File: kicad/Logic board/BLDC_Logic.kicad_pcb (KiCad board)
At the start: 2 copper layers, 82.2 x 79.8 mm, 46 parts, among them J1 CONN_01X03, J10 Encdr Pwr, J11 3ph board, J12 3v3 output, J13 3v3 output, J2 CMD inputs, J3 IO, J4 CONN_01X03, J5 5V output, J6 5V output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

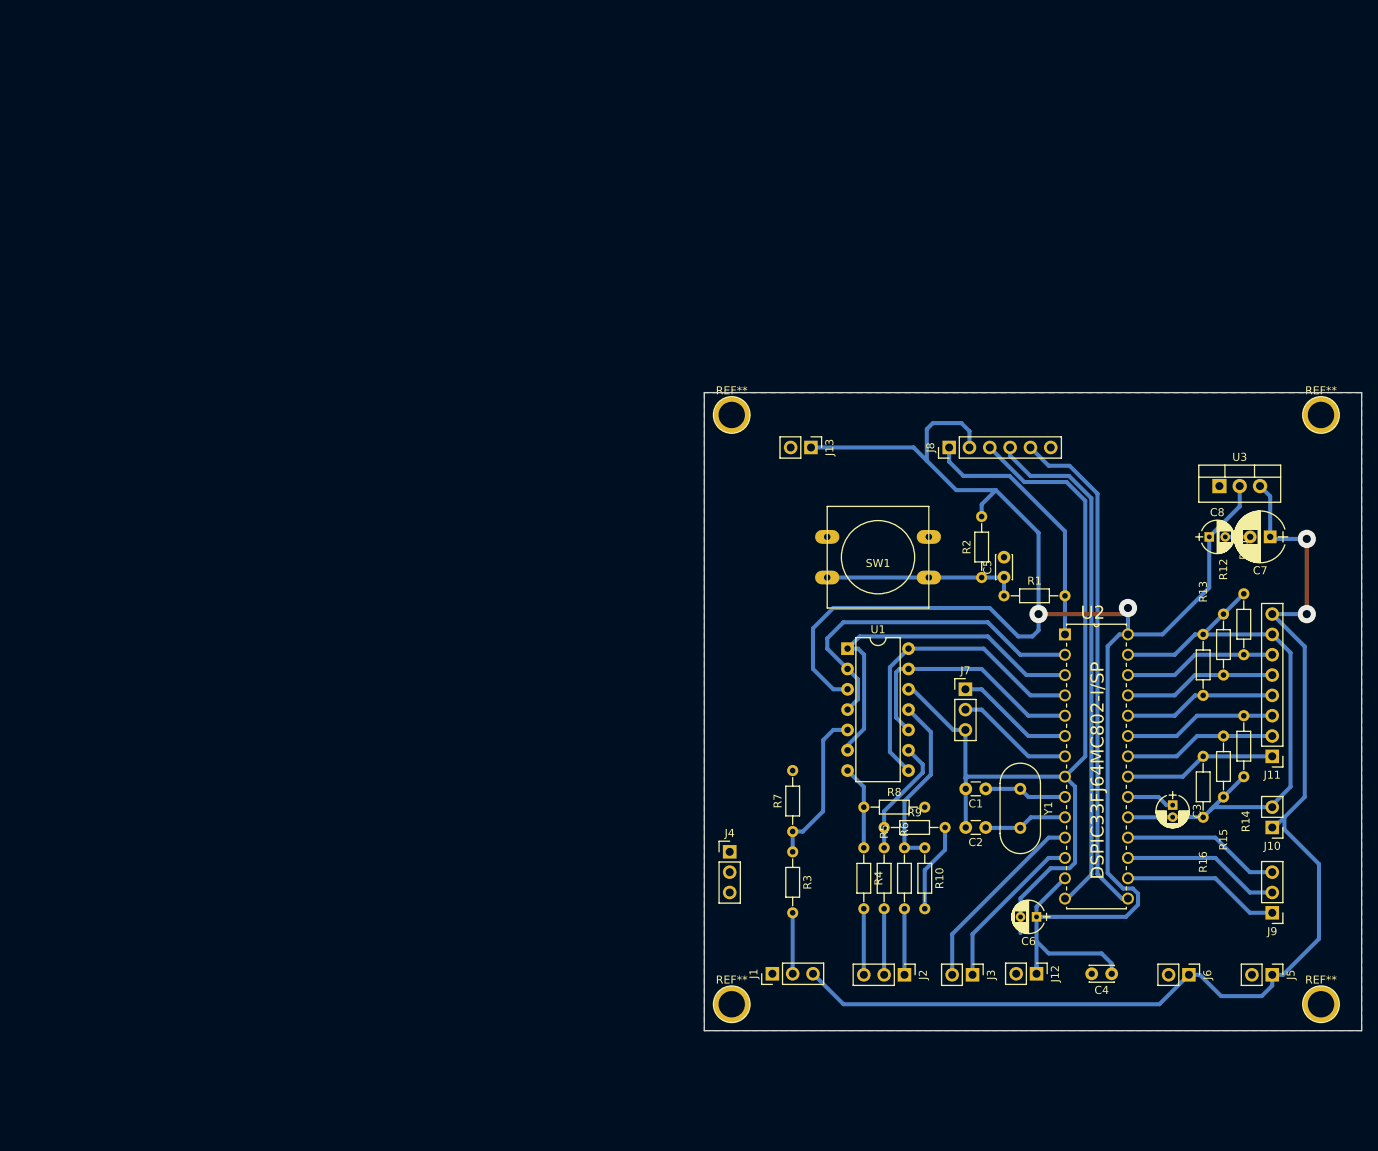
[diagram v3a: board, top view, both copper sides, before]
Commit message: changed the botton to better fit components. thickened traces for easier PCB fabrication. did some minor rerouting for smaller current loops.
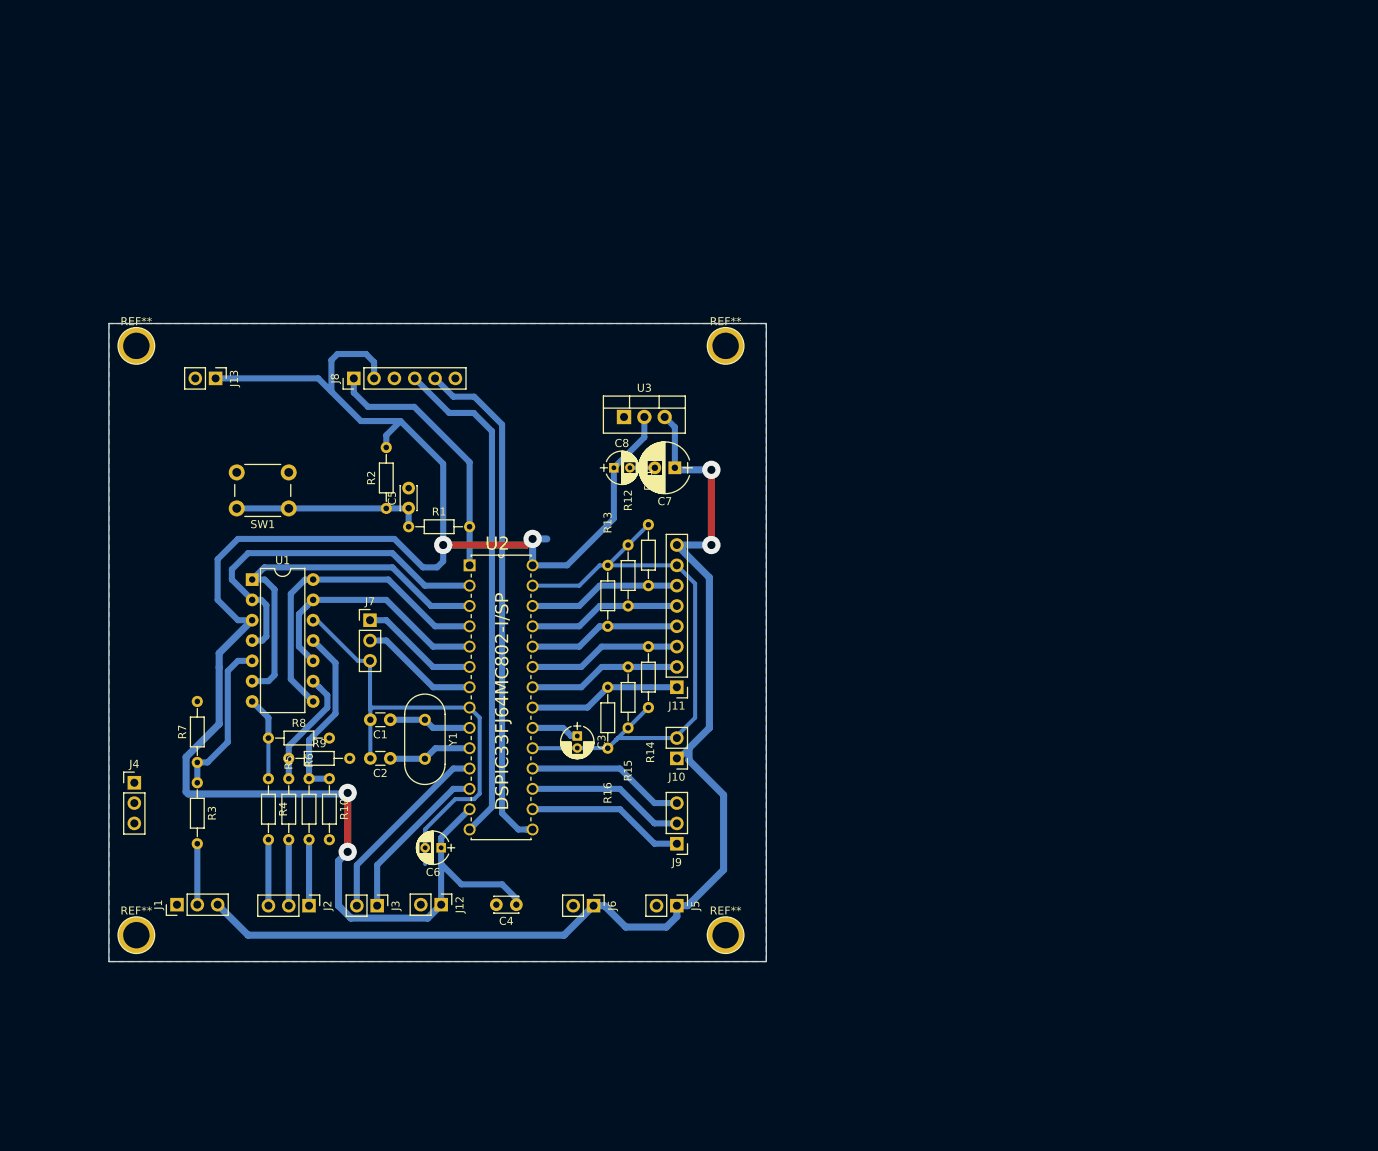
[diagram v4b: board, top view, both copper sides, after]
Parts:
- SW1: footprint Buttons_Switches_THT:SW_PUSH-12mm -> Buttons_Switches_THT:SW_PUSH_6mm
- moved C4 74.9 mm to (104.9, 129.5)
- moved J3 74.9 mm to (87.5, 129.7)
- moved R12 74.9 mm to (118.9, 92.2)
- moved R15 74.9 mm to (118.9, 99.8)
- moved R2 74.9 mm to (88.6, 80.0)
- moved R4 74.9 mm to (73.9, 113.8)
- moved R5 74.9 mm to (76.5, 113.8)
- moved R8 74.9 mm to (73.9, 108.7)
- moved R9 74.9 mm to (76.5, 111.3)
- moved Y1 74.9 mm to (93.5, 106.4)
- moved C1 74.9 mm to (89.2, 106.4)
- moved C2 74.9 mm to (89.2, 111.3)
- moved C5 74.9 mm to (91.4, 80.0)
- moved C7 74.9 mm to (124.7, 74.9)
- moved C8 74.9 mm to (117.1, 74.9)
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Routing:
- net GND: track 196.9 -> 135.4 mm
- net +3V3: track 220.7 -> 245.7 mm, vias 2 -> 4
- net /O2: track 45.0 -> 46.9 mm
- net /O1: track 43.3 -> 45.1 mm
- net Net-(J8-Pad4): track 65.0 -> 63.6 mm
- net /O3: track 39.1 -> 40.1 mm
- net Net-(J8-Pad5): track 63.4 -> 64.0 mm
- net Net-(C5-Pad1): track 24.4 -> 23.9 mm
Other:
- net class Default: trace_width 0.25 -> 0.762; via_dia 0.6 -> 2.286; via_drill 0.4 -> 1.016
- net class Power added: clearance 0.254, trace_width 0.889, via_dia 2.286, via_drill 1.016
